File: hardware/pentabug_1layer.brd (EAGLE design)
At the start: 82.9 x 33 mm, 17 parts, among them IC1 ATMEGA88

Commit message: some routin
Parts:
- moved C3 1.30 mm to (45.1, 9.40)
- moved JP2 0.76 mm to (74.9, 28.4)
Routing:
- net BUZZR: track 0.00 -> 20.8 mm
- net VIBRATE: track 43.2 -> 54.8 mm, vias 0 -> 2
- net MISO: track 28.3 -> 19.9 mm
- net GND: track 43.3 -> 35.1 mm, vias 16 -> 11
- net VCC: track 162.6 -> 154.4 mm
- net MOSI: track 29.0 -> 23.5 mm
- net BUZGND: track 43.7 -> 49.0 mm
- net RX: track 47.1 -> 52.3 mm
- net TX: track 107.8 -> 112.3 mm
- net RST: track 75.5 -> 72.0 mm
- net N$23: track 1.27 -> 0.00 mm
- net SCK: track 37.4 -> 38.2 mm

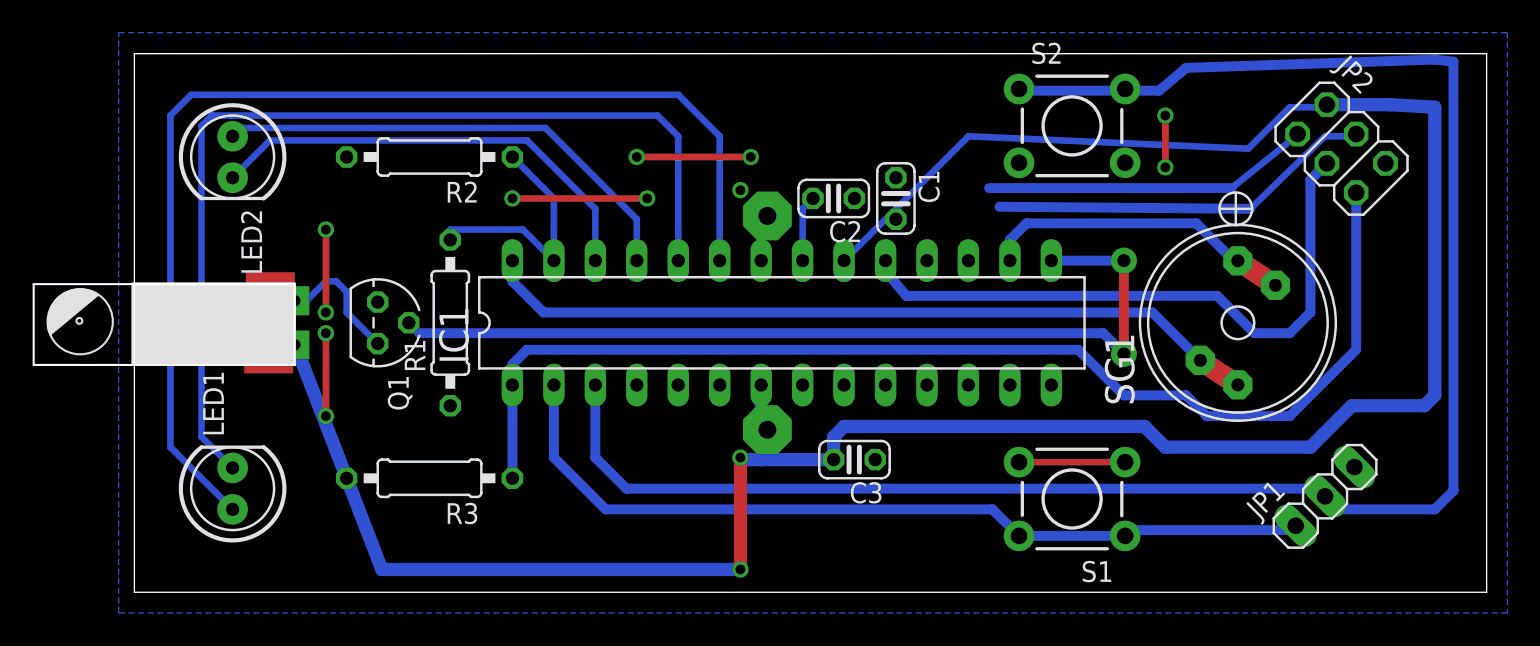
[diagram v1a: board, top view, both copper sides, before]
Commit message: stil not satisfied with routing for 1 layer board
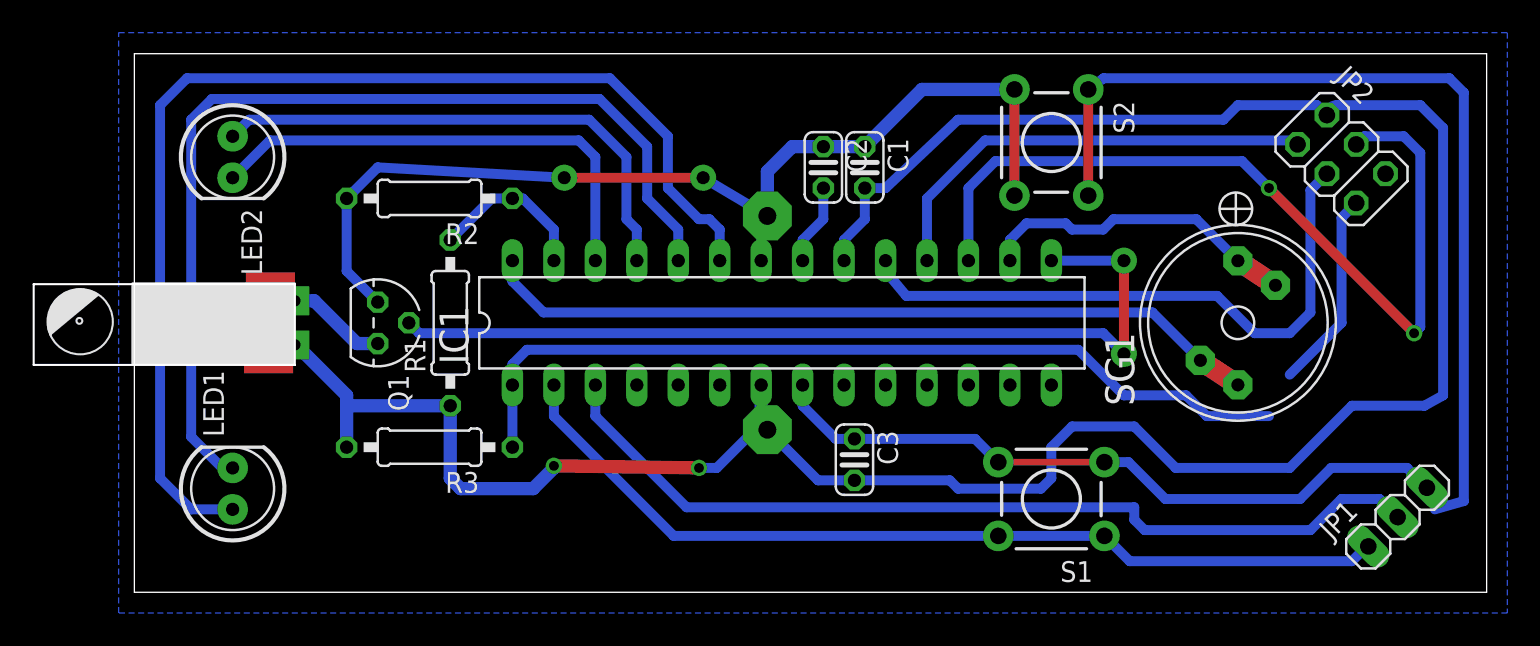
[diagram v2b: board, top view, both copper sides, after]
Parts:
- moved JP1 4.62 mm to (78.4, 5.88)
- moved C1 2.69 mm to (45.7, 27.3)
- moved R2 2.54 mm to (19.1, 25.4)
- moved C2 2.01 mm to (43.2, 27.3), turned to 270 degrees
- moved R3 1.90 mm to (19.1, 10.2)
- moved S2 1.63 mm to (57.1, 28.8), turned to 270 degrees
- moved S1 1.27 mm to (57.1, 6.99)
- moved JP2 0.64 mm to (74.9, 27.8)
- turned C3 to 270 degrees
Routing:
- net GND: track 35.1 -> 106.9 mm, vias 11 -> 2
- net MOSI: track 23.5 -> 52.6 mm, vias 0 -> 2
- net MISO: track 19.9 -> 28.1 mm
- net RST: track 72.0 -> 65.7 mm
- net BATLVL: track 15.2 -> 10.1 mm
- net VCC: track 154.4 -> 150.7 mm
- net RX: track 52.3 -> 55.9 mm
- net N$5: track 29.8 -> 32.1 mm
- net N$3: track 68.6 -> 70.7 mm
- net BATTLVL: track 28.1 -> 29.9 mm
- net N$8: track 7.90 -> 6.17 mm
- net N$17: track 4.07 -> 4.97 mm
- net N$10: track 59.4 -> 60.2 mm
- net BUZZR: track 20.8 -> 21.6 mm
- net SCK: track 38.2 -> 37.6 mm

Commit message: routing finished
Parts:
- moved JP1 1.91 mm to (78.4, 7.78)
- moved S1 1.14 mm to (57.1, 8.13)
- moved C3 0.25 mm to (45.1, 9.65)
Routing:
- net GND: track 106.9 -> 224.2 mm, vias 2 -> 4
- net VCC: track 150.7 -> 146.2 mm
- net RST: track 65.7 -> 68.8 mm
- net TX: track 112.6 -> 114.0 mm
- added copper zone on layer 16, net N$1
- added copper zone on layer 16, net N$2
- removed copper zone on layer 16, net GND
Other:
- board text added: "Pentabug 0.1"

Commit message: modified to use biggr buzzr - routing not adapted yet!
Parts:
- SG1: value MULTIBUZZR -> MULTIBUZZRTDKBUZZR; device buglbr:MULTIBUZZR -> buglbr:BUZZRTDK
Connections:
- net BUZGND: no longer SG1.-1
- net BUZZR: no longer SG1.+1
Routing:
- net BUZZR: track 21.6 -> 23.2 mm
- net BUZGND: track 49.0 -> 50.4 mm
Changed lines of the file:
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@@
 <element name="JP2" library="pinhead" package="2X03" value="" x="74.93" y="27.813" rot="R315"/>
 <element name="U$1" library="buglbr" package="LA4-432" value="VIBRAMOTOR" x="3.81" y="17.78" rot="R180"/>
-<element name="SG1" library="buglbr" package="MULTIBUZZR" value="MULTIBUZZR" x="68.58" y="17.78" rot="R90">
-<attribute name="OC_NEWARK" value="unknown" x="68.58" y="17.78" size="1.778" layer="27" rot="R90" display="off"/>
-<attribute name="MPN" value="" x="68.58" y="17.78" size="1.778" layer="27" rot="R90" display="off"/>
-<attribute name="MF" value="" x="68.58" y="17.78" size="1.778" layer="27" rot="R90" display="off"/>
-<attribute name="OC_FARNELL" value="unknown" x="68.58" y="17.78" size="1.778" layer="27" rot="R90" display="off"/>
-</element>
+<element name="SG1" library="buglbr" package="BUZZRTDK" value="MULTIBUZZRTDKBUZZR" x="68.58" y="17.78" rot="R90"/>
 <element name="R1" library="rcl" package="0207/10" value="100K" x="20.32" y="17.78" rot="R90"/>
 <element name="R2" library="rcl" package="0207/10" value="18K" x="19.05" y="25.4" rot="R180"/>
@@
 <signal name="BUZZR">
 <contactref element="IC1" pad="16"/>
-<contactref element="SG1" pad="+1"/>
 <contactref element="SG1" pad="+"/>
-<wire x1="68.58" y1="21.58" x2="69.38" y2="21.58" width="0.4064" layer="16"/>
-<wire x1="68.58" y1="22.225" x2="68.58" y2="21.58" width="0.4064" layer="16"/>
-<wire x1="70.88" y1="20.08" x2="68.58" y2="21.58" width="0.8128" layer="16"/>
+<wire x1="68.58" y1="22.78" x2="69.38" y2="21.58" width="0.4064" layer="16"/>
+<wire x1="68.58" y1="22.225" x2="68.58" y2="22.78" width="0.4064" layer="16"/>
+<wire x1="70.88" y1="20.08" x2="68.58" y2="22.78" width="0.8128" layer="16"/>
 <wire x1="54.61" y1="21.59" x2="54.61" y2="22.86" width="0.6096" layer="16"/>
 <wire x1="55.626" y1="23.876" x2="58.029" y2="23.876" width="0.6096" layer="16"/>
-<wire x1="68.326" y1="21.58" x2="68.58" y2="21.58" width="0.6096" layer="16"/>
+<wire x1="68.326" y1="21.58" x2="68.58" y2="22.78" width="0.6096" layer="16"/>
 <wire x1="58.029" y1="23.876" x2="58.41" y2="23.495" width="0.6096" layer="16"/>
 <wire x1="58.41" y1="23.495" x2="60.325" y2="23.495" width="0.6096" layer="16"/>
@@
 <wire x1="60.96" y1="24.13" x2="66.03" y2="24.13" width="0.6096" layer="16"/>
 <wire x1="54.61" y1="22.86" x2="55.626" y2="23.876" width="0.6096" layer="16"/>
-<wire x1="66.03" y1="24.13" x2="68.58" y2="21.58" width="0.6096" layer="16"/>
+<wire x1="66.03" y1="24.13" x2="68.58" y2="22.78" width="0.6096" layer="16"/>
 </signal>
 <signal name="VIBRATE">
@@
 <signal name="BUZGND">
 <contactref element="IC1" pad="28"/>
-<contactref element="SG1" pad="-1"/>
 <contactref element="SG1" pad="-"/>
 <wire x1="26.035" y1="18.415" x2="63.345" y2="18.415" width="0.6096" layer="16"/>
-<wire x1="68.58" y1="13.98" x2="67.78" y2="13.98" width="0.4064" layer="16"/>
+<wire x1="68.58" y1="12.78" x2="67.78" y2="13.98" width="0.4064" layer="16"/>
 <wire x1="26.035" y1="18.415" x2="24.13" y2="20.32" width="0.6096" layer="16"/>
 <wire x1="24.13" y1="20.32" x2="24.13" y2="21.59" width="0.6096" layer="16"/>
-<wire x1="66.28" y1="15.48" x2="68.58" y2="13.98" width="0.8128" layer="16"/>
+<wire x1="66.28" y1="15.48" x2="68.58" y2="12.78" width="0.8128" layer="16"/>
 <wire x1="63.345" y1="18.415" x2="66.28" y2="15.48" width="0.6096" layer="16"/>
 </signal>
